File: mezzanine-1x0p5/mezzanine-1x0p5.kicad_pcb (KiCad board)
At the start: 2 copper layers, 14 x 16 mm, 11 parts

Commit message: create 1xp5 panel
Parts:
- C101, C102, C103, C104, C105, C106, C107, C108: value C_Small -> 1uF

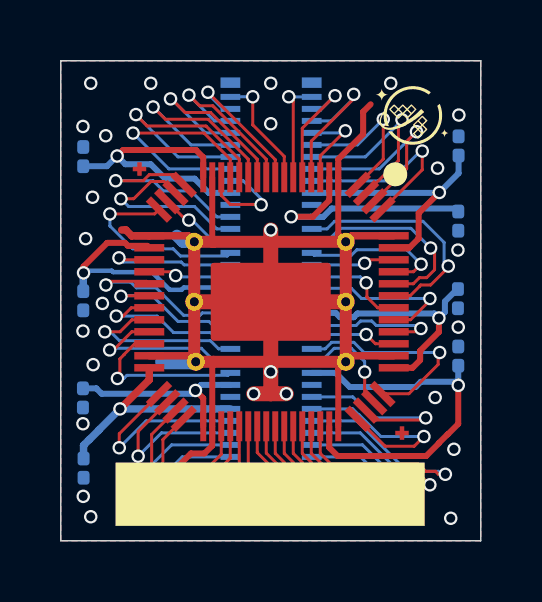
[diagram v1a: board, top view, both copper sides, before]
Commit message: more clearance for 1xp5
PCB house complained about clearance, kicad file was created with exact clearance. I reduced it so we should be good.
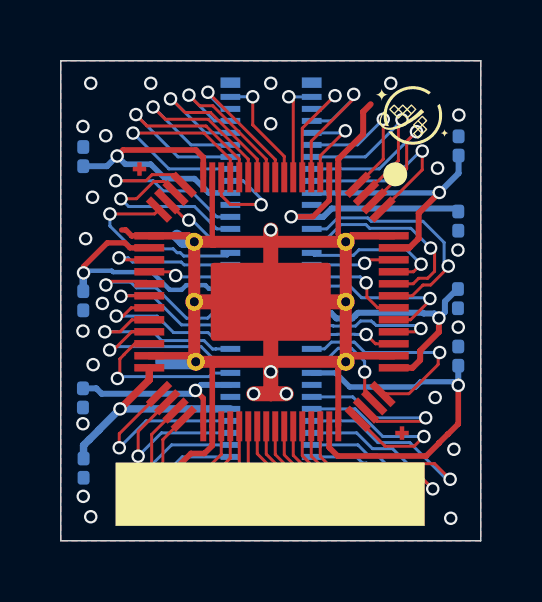
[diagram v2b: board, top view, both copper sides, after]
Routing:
- net /bidir_41: track 10.6 -> 11.1 mm
